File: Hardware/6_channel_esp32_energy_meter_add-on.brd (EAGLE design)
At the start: 61 x 62.2 mm, 105 parts, among them IC1 ATM90E32AS, IC2 ATM90E32AS, J16 PINHD-1X19, J4 TMM-103-01-T-D-SM, J5 PINHD1X1-SM1X01_SM, J6 PINHD1X1-SM1X01_SM, J7 TMM-103-01-T-D-SM, J8 PINHD1X1-SM1X01_SM, U1 ESP32-DEVKITC-32D, Y1 16.384MHz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

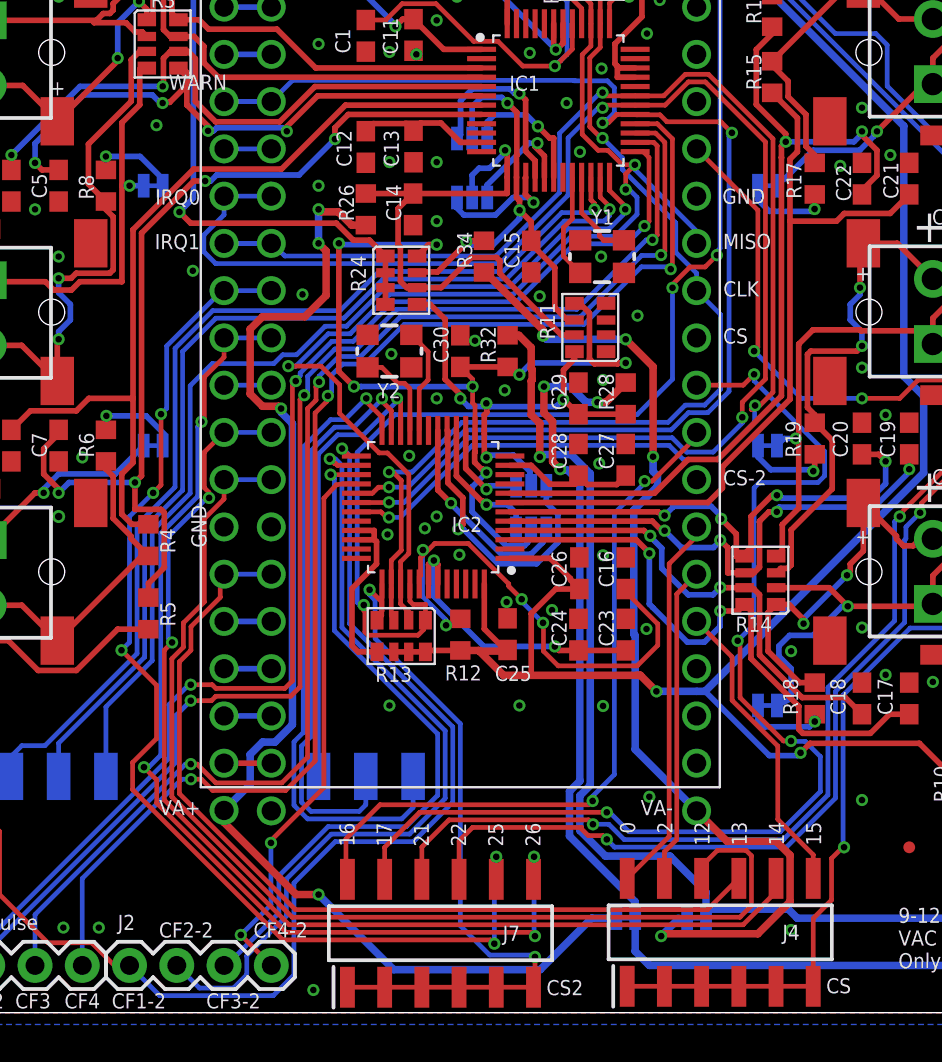
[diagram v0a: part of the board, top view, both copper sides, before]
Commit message: v1.3 rev2
– Added voltage divider on ground for voltage channel 2
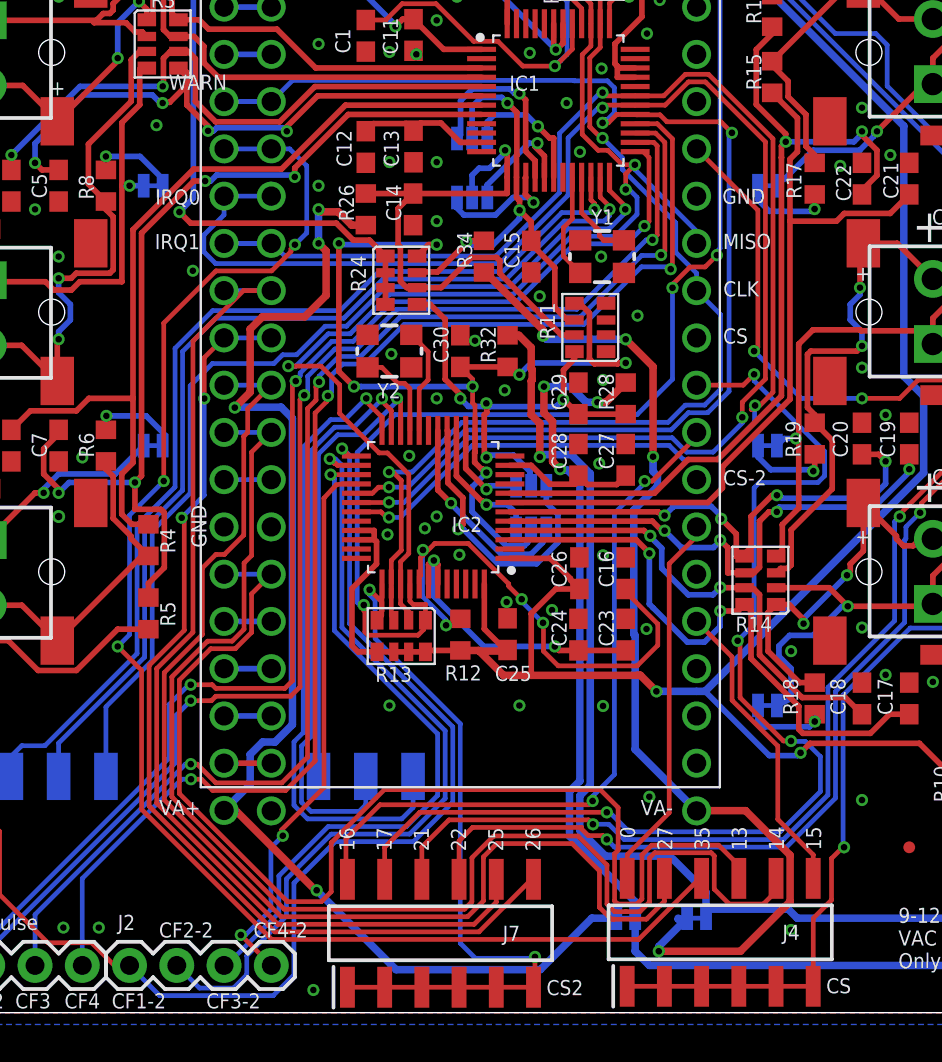
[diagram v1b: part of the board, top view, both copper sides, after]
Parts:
- R14: value 1K -> 100
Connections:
- net IO12: no longer J4.10
- net IO2: no longer J4.11
- net IO27: now also J4.11
- net IO35: now also J4.10
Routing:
- net IO35: track 2.54 -> 80.3 mm, vias 0 -> 3
- net IO27: track 2.54 -> 64.4 mm
- net IO12: track 61.3 -> 2.54 mm
- net IO2: track 17.1 -> 0.00 mm
- net IO13: track 48.7 -> 63.3 mm
- net IO14: track 61.2 -> 71.9 mm, vias 2 -> 0
- net IO25: track 61.9 -> 56.2 mm, vias 5 -> 0
- net IO26: track 58.6 -> 54.1 mm, vias 4 -> 2
- net VA-: track 55.3 -> 56.9 mm
- net VA+: track 67.9 -> 69.2 mm
- net !CS-2: track 40.5 -> 41.1 mm
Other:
- board text added: "0 27 35 13 14 15"
- board text removed: "0 2 12 13 14 15"

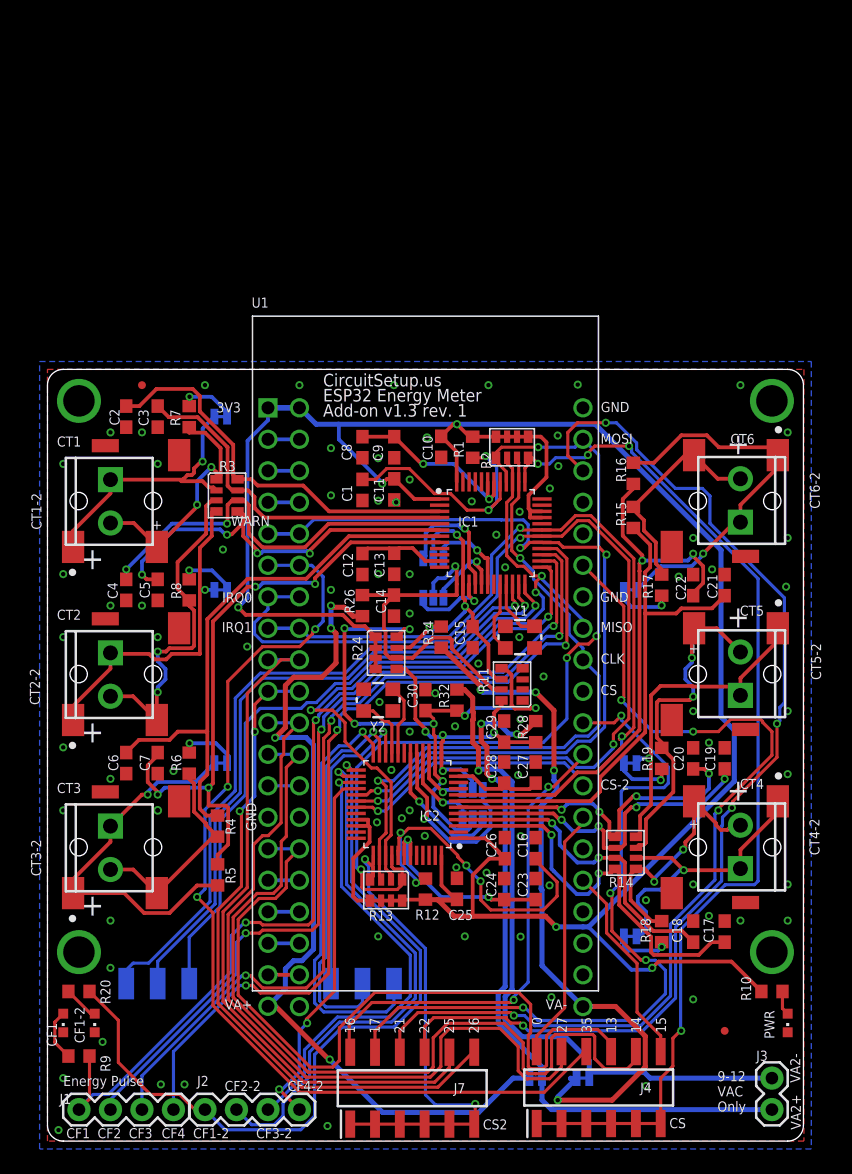
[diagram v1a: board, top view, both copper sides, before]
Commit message: v1.4
- Added optional micro-hdmi connection to connect the current transformer remote board. This allows for all 6 current transformer connections to connect to a remote pcb, which then connects to the main board via 1 micro-hdmi cable. Instead of 6 wires coming out of the meter, there can now be 1.
- Added current transformer remote pcb
- Removed JP8-JP11 and connected all voltage channels together for each ATM90E32
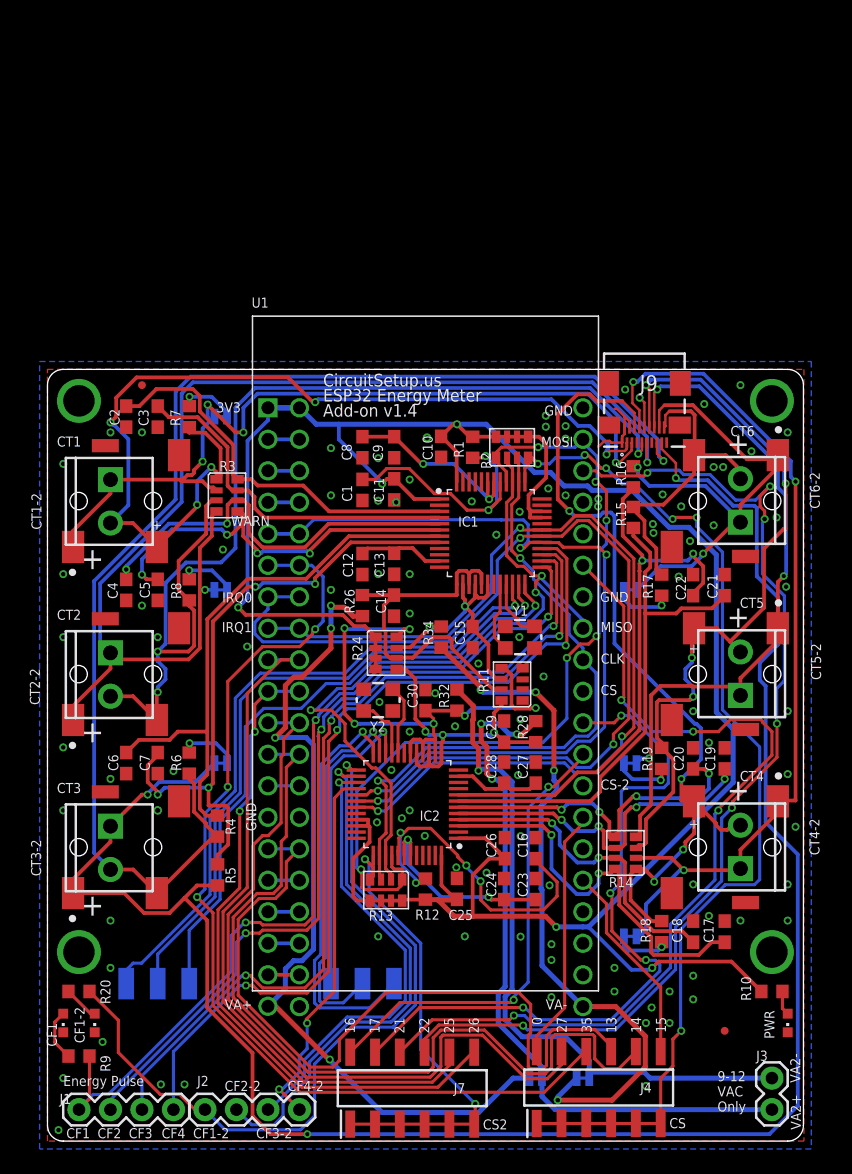
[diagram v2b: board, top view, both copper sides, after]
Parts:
- removed JP10, JP11, JP8, JP9: JUMPER-SMT_3_NO_SILK, SparkFun-Jumpers:SMT-JUMPER_3_NO_SILK
- added J9: 46765-0001, 46765-0001:46765-0001
- moved R16 0.28 mm to (47.2, 32.0)
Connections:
- removed net V2N: IC1.16, JP9.3
- removed net V2N-2: IC2.16, JP11.3
- removed net V2P: IC1.15, JP8.3
- removed net V2P-2: IC2.15, JP10.3
- removed net V3N: IC1.18, JP9.1
- removed net V3N-2: IC2.18, JP11.1
- removed net V3P: IC1.17, JP8.1
- removed net V3P-2: IC2.17, JP10.1
- net GND: now also J9.1, J9.10, J9.13, J9.2, J9.4, J9.7
- net IA+: now also J9.3
- net IA+-2: now also J9.6
- net IA-: now also J9.5
- net IA--2: now also J9.8
- net IB+: now also J9.9
- net IB+-2: now also J9.12
- net IB-: now also J9.11
- net IB--2: now also J9.14
- net IC+: now also J9.15
- net IC+-2: now also J9.18
- net IC-: now also J9.17
- net IC--2: now also J9.16
- net VAN: now also IC1.16, IC1.18; no longer JP9.2
- net VAN2: now also IC2.16, IC2.18; no longer JP11.2
- net VAP: now also IC1.15, IC1.17; no longer JP8.2
- net VAP2: now also IC2.15, IC2.17; no longer JP10.2
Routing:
- net IC-: track 30.5 -> 157.5 mm, vias 1 -> 3
- net IC+: track 17.3 -> 104.2 mm, vias 0 -> 1
- net IB-: track 27.8 -> 94.6 mm, vias 1 -> 2
- net IB+: track 27.5 -> 88.6 mm, vias 2 -> 3
- net IA+: track 20.2 -> 77.6 mm, vias 2 -> 5
- net IA+-2: track 20.7 -> 69.2 mm, vias 2 -> 4
- net IA--2: track 24.1 -> 71.7 mm, vias 1 -> 3
- net IA-: track 22.5 -> 66.6 mm, vias 1 -> 4
- net IB+-2: track 27.2 -> 61.6 mm, vias 2 -> 4
- net IB--2: track 27.7 -> 57.1 mm, vias 1 -> 3
- net V3P-2: track 15.7 -> 0.00 mm, vias 1 -> 0
- net V3N-2: track 11.4 -> 0.00 mm, vias 1 -> 0
- net IC--2: track 30.6 -> 41.3 mm, vias 1 -> 2
- net V2N: track 10.5 -> 0.00 mm, vias 1 -> 0
- net GND: track 0.00 -> 9.06 mm, vias 92 -> 107
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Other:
- board text added: "CircuitSetup.us ESP32 Energy Meter Add-on v1.4"
- board text removed: "CircuitSetup.us ESP32 Energy Meter Add-on v1.3 rev. 1"
- board text removed: "JP8 - JP11: Connect the center pad with the 2 outer pads to connect all 3 voltage channels together for each IC"

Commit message: Updated Eagle files to v1.4 rev1
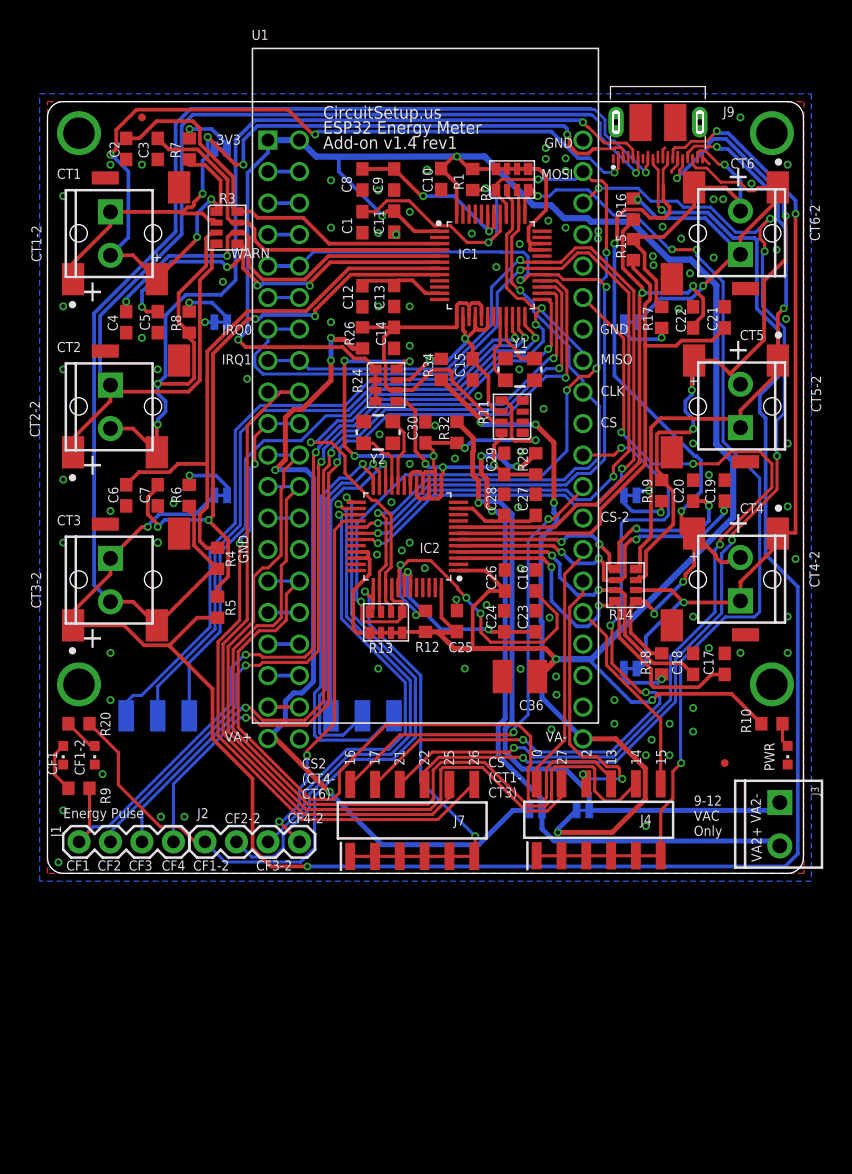
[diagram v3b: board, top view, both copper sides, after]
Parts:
- added C36: 100uF/6.3V/1210, rcl:C1210
- J3: device SparkFun-Connectors:1X02 -> SparkFun-Connectors:SCREWTERMINAL-3.5MM-2
- J9: value 46765-0001 -> PKS019-4011-0; device 46765-0001:46765-0001 -> SamacSys_Parts:PKS01940110
- moved J3 24.8 mm to (59.1, 5.71), turned to 270 degrees
- moved C1 21.6 mm to (25.4, 52.5)
- moved C10 21.6 mm to (31.8, 56.0)
- moved C12 21.6 mm to (25.4, 46.5)
- moved C2 21.6 mm to (6.35, 58.4)
- moved C21 21.6 mm to (54.6, 44.8)
- moved C22 21.6 mm to (52.1, 44.8)
- moved C29 21.6 mm to (36.8, 33.0)
- moved C3 21.6 mm to (8.89, 58.4)
- moved C30 21.6 mm to (30.5, 35.6)
- moved C4 21.6 mm to (6.35, 44.5)
- moved C5 21.6 mm to (8.89, 44.5)
- moved C8 21.6 mm to (25.4, 56.0)
- moved C9 21.6 mm to (28.0, 56.0)
- moved CT1 21.6 mm to (5.08, 53.3)
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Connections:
- net GND: now also C36.2, J9.11, J9.14, J9.19, J9.21, J9.22, J9.P$1, J9.P$2; no longer J9.13, J9.2
- net IA+: now also J9.2; no longer J9.3
- net IA+-2: now also J9.12; no longer J9.6
- net IA-: now also J9.3; no longer J9.5
- net IA--2: now also J9.13; no longer J9.8
- net IB+: now also J9.5; no longer J9.9
- net IB+-2: now also J9.15; no longer J9.12
- net IB-: now also J9.6; no longer J9.11
- net IB--2: now also J9.16; no longer J9.14
- net IC+: now also J9.8; no longer J9.15
- net IC-: now also J9.9; no longer J9.17
- net IC--2: now also J9.17; no longer J9.16
- net IO2: now also J4.10
- net IO35: no longer J4.10
- net VA2+: now also J3.2; no longer J3.1
- net VA2-: now also J3.1; no longer J3.2
- net VDD: now also C36.1
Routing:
- net IO35: track 80.3 -> 2.54 mm, vias 3 -> 0
- net IO2: track 0.00 -> 23.6 mm, vias 0 -> 2
- net IA+-2: track 69.2 -> 60.7 mm
- net IA--2: track 71.7 -> 64.7 mm
- net IB--2: track 57.1 -> 50.9 mm
- net GND: track 9.06 -> 3.74 mm, vias 107 -> 104
- net IC--2: track 41.3 -> 36.3 mm
- net IB+-2: track 61.6 -> 57.5 mm
- net IA-: track 66.6 -> 63.2 mm
- net IB+: track 88.6 -> 85.9 mm
- net IC+: track 104.2 -> 101.7 mm
- net IB-: track 94.6 -> 92.2 mm
- net VDD: track 207.3 -> 209.7 mm
- net IC-: track 157.5 -> 159.8 mm
- net IA+: track 77.6 -> 76.1 mm
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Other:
- board text added: "0 27 2 13 14 15"
- board text added: "CS (CT1- CT3)"
- board text added: "CS2 (CT4- CT6)"
- board text added: "CircuitSetup.us ESP32 Energy Meter Add-on v1.4 rev1"
- board text added: "NOTE: To measure voltage & power this board, a main board energy meter is required. For detailed documentation, please visit CircuitSetup.us"
- board text added: "Sever JP12 & JP13 to use VA2+ as secondary voltage measurement input. VA2+ should be hooked up to a second 9-12 VAC transformer on a different phase than the main board primary transformer. DO NOT connect both without severing these connections first!"
- board text removed: "0 27 35 13 14 15"
- board text removed: "3V3 OUT"
- board text removed: "CS2"
- board text removed: "CircuitSetup.us ESP32 Energy Meter Add-on v1.4"
- board text removed: "NOTE: A 9 to 12V AC transformer is required to measure voltage and power this board. Do NOT input more than 12VAC For detailed documentation, please visit CircuitSetup.us"
- board text removed: "Sever JP12 & JP13 to use VA2+ as secondary voltage measurement input. VA2+ should be hooked up to a second AC transformer on a different phase than the main board primary transformer. DO NOT connect both without severing these connections first!"
